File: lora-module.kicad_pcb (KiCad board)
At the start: 4 copper layers, 50 parts, among them J101 Conn_Coaxial, J102 Conn_ARM_SWD_TagConnect_TC203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, Q101 PMN48XP, U201 STM32WLE5CCUx, U301 BALFHB-WL-05D3, U302 BGS12SN6E6327XTSA1, U401 SST26VF080A

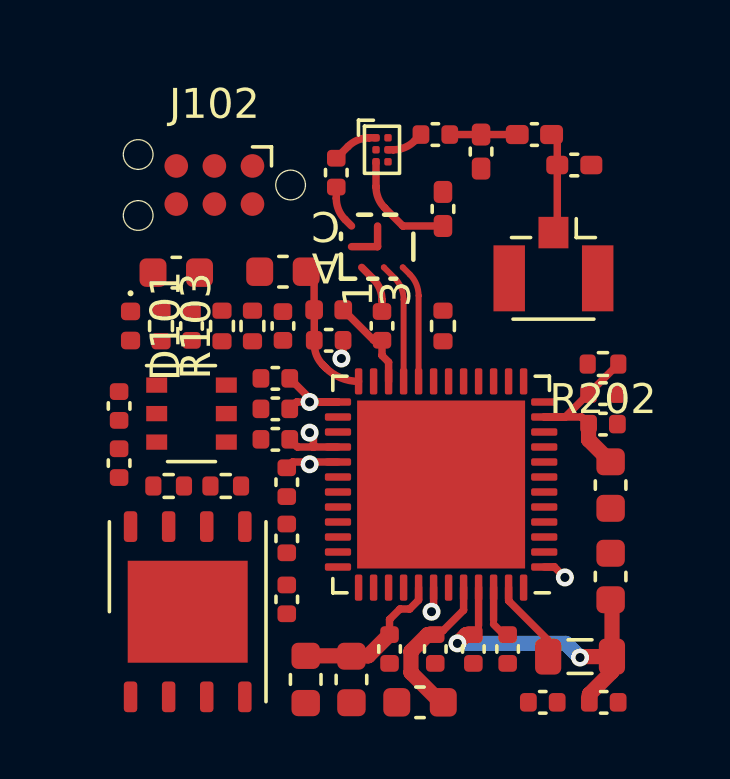
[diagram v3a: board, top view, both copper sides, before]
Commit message: added the crystal
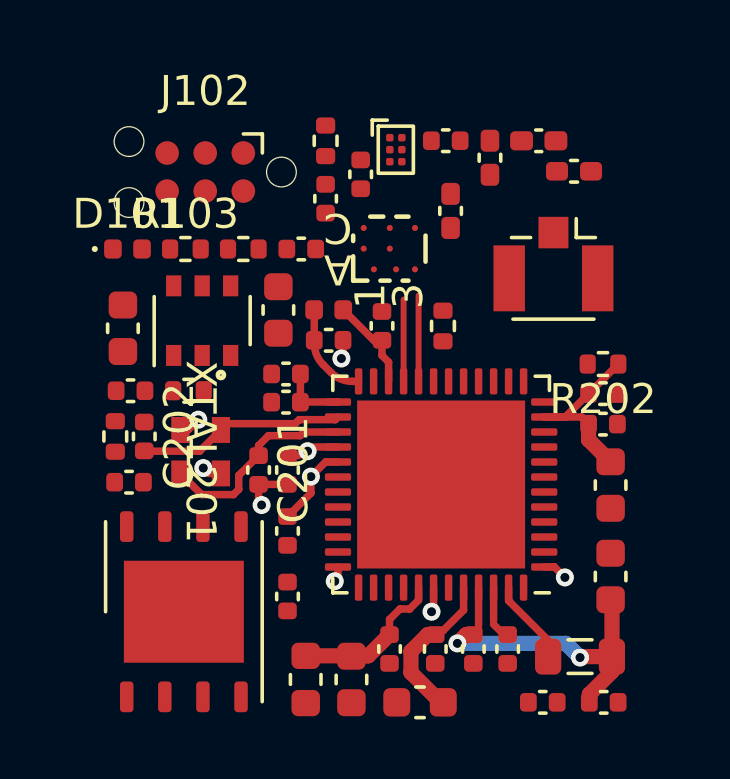
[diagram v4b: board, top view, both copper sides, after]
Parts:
- added C201: 6.8p, Capacitor_SMD:C_0402_1005Metric, F.Cu at (131.3, 101.4)
- added XTAL201: NX2016SA-32MHZ-EXS00A-CS11336, lora-module:NX2016SA_NDK, F.Cu at (129.3, 100.8)
- C202: value 100n -> 6.8
- moved C202 7.21 mm to (127.5, 100.3)
- moved R301 7.07 mm to (133.5, 90.5), turned to -90 degrees
- moved C307 6.16 mm to (133.5, 92.4)
- moved R102 3.41 mm to (128.9, 98.8)
- moved Q101 3.12 mm to (129.4, 96.5), turned to 90 degrees
- moved R103 2.69 mm to (128.8, 94.1), turned to 0 degrees
- moved C309 2.64 mm to (132.7, 94.1), turned to 0 degrees
- moved R302 2.58 mm to (130.8, 94.1), turned to 0 degrees
- moved C101 2.57 mm to (126.7, 96.7), turned to 90 degrees
- moved D101 2.57 mm to (126.9, 94.1), turned to 0 degrees
- moved R101 2.43 mm to (126.5, 100.3), turned to -90 degrees
- moved C204 1.94 mm to (132.2, 105.7)
- moved C213 1.63 mm to (132.2, 103.5)
- moved C301 1.28 mm to (131.9, 96.1), turned to 90 degrees
- moved C209 1.10 mm to (132.2, 101.4), turned to -90 degrees
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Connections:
- C202 pad 1: /STM32WL/VBAT -> GND
- C202 pad 2: GND -> Net-(U201-OSC_IN)
- U201 pad 26: unconnected-(U201-OSC_IN-Pad26) -> Net-(U201-OSC_IN)
- U201 pad 27: unconnected-(U201-OSC_OUT-Pad27) -> Net-(U201-OSC_OUT)
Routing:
- net Net-(U201-OSC_IN): track 0.00 -> 6.93 mm
- net Net-(U201-OSC_OUT): track 0.00 -> 6.88 mm
- net Net-(U301-RFI_IN): track 3.80 -> 0.00 mm
- net /RF frontend/RF_ANT: track 3.71 -> 0.00 mm
- net Net-(C310-Pad2): track 2.25 -> 0.00 mm
- net Net-(U301-RFO_IN): track 1.70 -> 0.00 mm
- net Net-(U302-RF2): track 1.56 -> 0.00 mm
- net GND: track 2.19 -> 3.73 mm, vias 1 -> 4
- net Net-(U301-RFO_OUT): track 1.46 -> 0.00 mm
- net /RF frontend/VR_PA: track 4.63 -> 3.27 mm
- net /RF frontend/RFI_N: track 4.02 -> 2.73 mm
- net Net-(U302-RF): track 1.26 -> 0.00 mm
- net /RF frontend/RFI_P: track 3.97 -> 2.86 mm
- net /STM32WL/VDDPA: track 16.8 -> 16.1 mm, vias 4 -> 3
- net /STM32WL/SWDIO: track 0.00 -> 0.52 mm, vias 0 -> 1

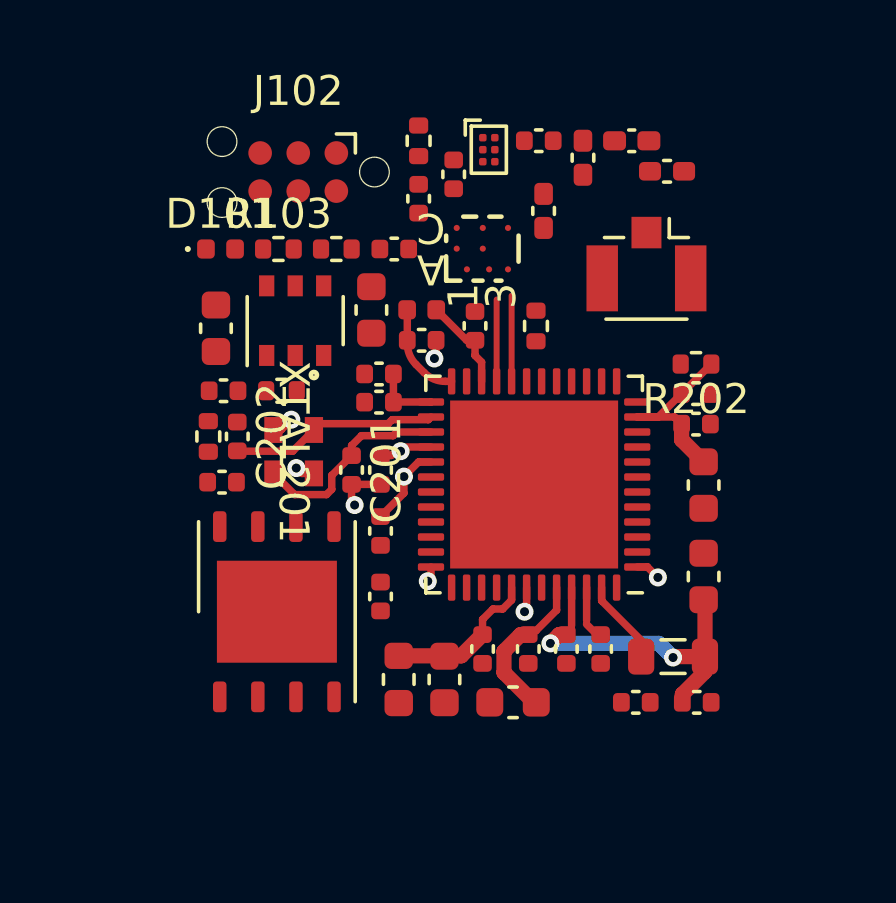
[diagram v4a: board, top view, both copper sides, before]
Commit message: added castellated edge connectors
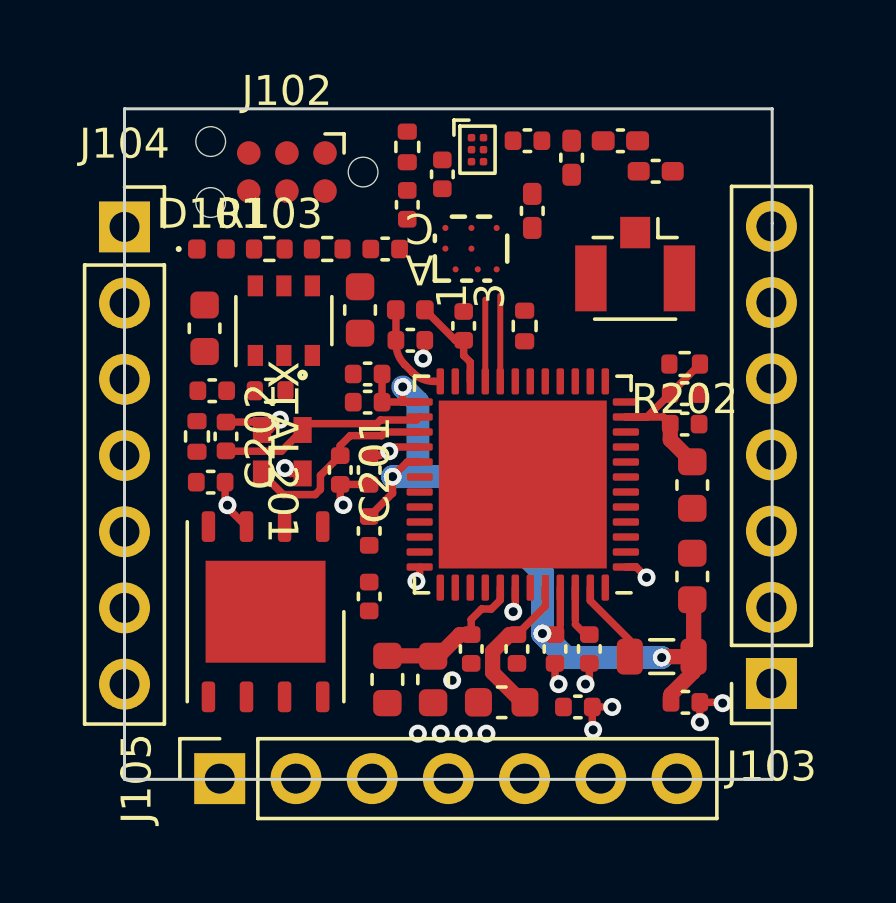
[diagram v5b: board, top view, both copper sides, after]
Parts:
- added J103: Conn_01x07_Socket, Connector_PinSocket_2.54mm:PinSocket_1x07_P2.54mm_Vertical, F.Cu at (145.3, 108.6)
- added J104: Conn_01x07_Socket, Connector_PinSocket_2.54mm:PinSocket_1x07_P2.54mm_Vertical, F.Cu at (123.7, 93.3)
- added J105: Conn_01x07_Socket, Connector_PinSocket_2.54mm:PinSocket_1x07_P2.54mm_Vertical, F.Cu at (126.9, 111.7)
- moved C218 1.94 mm to (138.8, 109.3)
- moved C307 0.43 mm to (133.1, 92.6)
- moved R301 0.43 mm to (133.1, 90.7)
- moved C201 0.38 mm to (130.9, 101.4)
- moved C203 0.38 mm to (136.3, 109.2)
- moved C204 0.38 mm to (131.9, 105.7)
- moved C209 0.38 mm to (131.9, 101.4)
- moved C210 0.38 mm to (135.3, 107.4)
- moved C211 0.38 mm to (142.6, 105.0)
- moved C213 0.38 mm to (131.9, 103.5)
- moved C214 0.38 mm to (142.6, 102.0)
- moved C215 0.38 mm to (131.8, 99.2)
- moved C217 0.38 mm to (131.8, 98.2)
- moved C220 0.38 mm to (136.8, 107.4)
- moved C301 0.38 mm to (131.5, 96.1)
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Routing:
- net /STM32WL/VDDPA: track 16.1 -> 28.8 mm, vias 3 -> 4
- net GND: track 3.73 -> 9.40 mm, vias 4 -> 15
- net VDD_SW: track 0.00 -> 1.85 mm, vias 0 -> 1
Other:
- board outline added: 21.6 x 22.4 mm

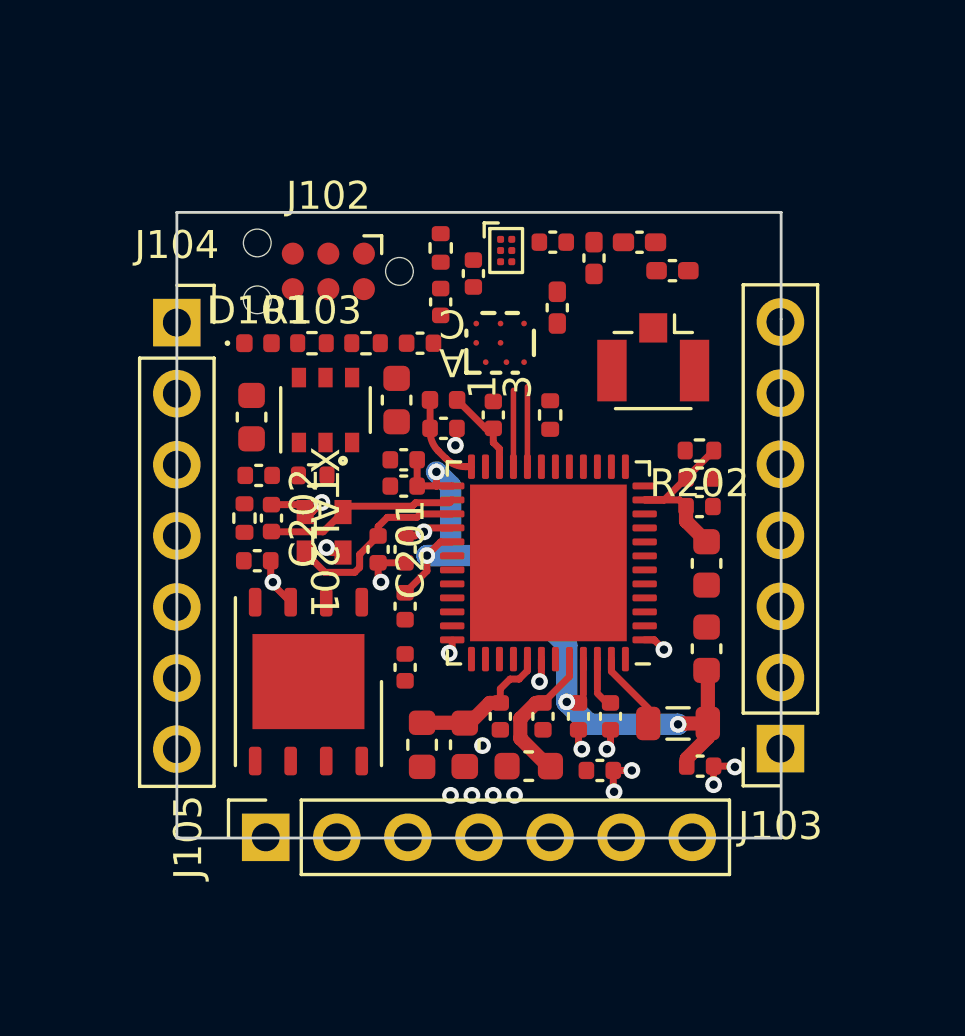
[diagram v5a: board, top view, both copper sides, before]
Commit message: created a footprint for the edge connectors
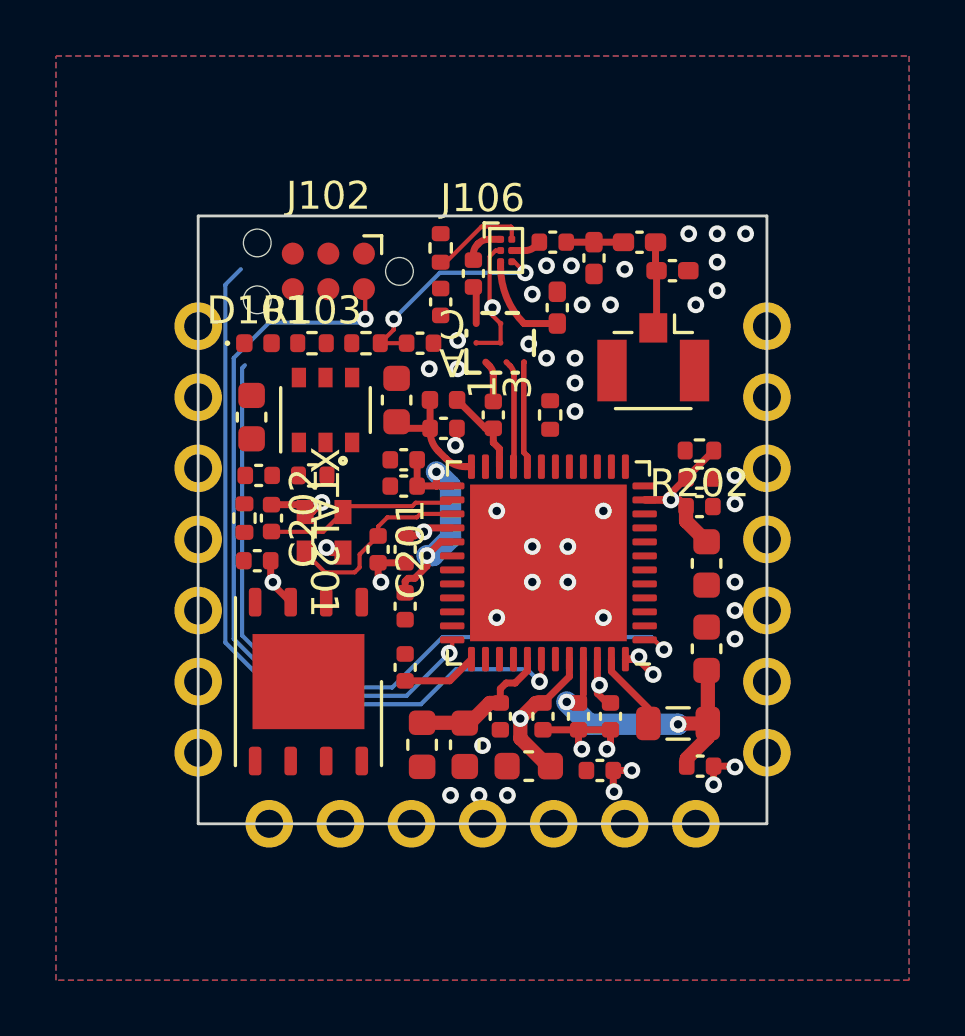
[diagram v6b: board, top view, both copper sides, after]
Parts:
- removed J103, J104, J105: Conn_01x07_Socket, Connector_PinSocket_2.54mm:PinSocket_1x07_P2.54mm_Vertical
- added J106: ~, lora-module:module-connectors, F.Cu at (134.6, 101.1)
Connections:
- net /STM32WL/BOOT0 renamed /BOOT0
- net /STM32WL/VBAT renamed /VBAT
- U201 pad 13: unconnected-(U201-PA5-Pad13) -> /FLASH/MISO
- U201 pad 16: unconnected-(U201-PA8-Pad16) -> /FLASH/SCK
- U201 pad 31: unconnected-(U201-PB2-Pad31) -> /FLASH/~{CS}
- U201 pad 32: unconnected-(U201-PB12-Pad32) -> /FLASH/~{HOLD}
- U201 pad 33: unconnected-(U201-PA10-Pad33) -> /FLASH/MOSI
- U401 pad 1: /EEPROM/~{CS} -> /FLASH/~{CS}
- U401 pad 2: /EEPROM/MISO -> /FLASH/MISO
- U401 pad 5: /EEPROM/MOSI -> /FLASH/MOSI
- U401 pad 6: /EEPROM/SCK -> /FLASH/SCK
- U401 pad 7: /EEPROM/~{HOLD} -> /FLASH/~{HOLD}
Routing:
- net /STM32WL/SWO: track 0.83 -> 27.3 mm
- net /STM32WL/SWCLK: track 0.83 -> 27.2 mm
- net /STM32WL/SWDIO: track 0.52 -> 26.1 mm, vias 1 -> 2
- net GND: track 9.40 -> 18.0 mm, vias 15 -> 48
- net Net-(U302-VDD): track 0.00 -> 8.03 mm, vias 0 -> 2
- net Net-(U301-RFI_IN): track 0.00 -> 3.60 mm
- net Net-(U302-CTRL): track 0.00 -> 3.51 mm
- net /RF frontend/RF_ANT: track 0.00 -> 3.12 mm
- net /VBAT: track 0.00 -> 2.69 mm
- net Net-(C310-Pad2): track 0.00 -> 2.05 mm
- net Net-(U301-RFO_IN): track 0.00 -> 1.49 mm
- net Net-(U302-RF2): track 0.00 -> 1.47 mm
- net Net-(U301-RFO_OUT): track 0.00 -> 1.35 mm
- net /RF frontend/VR_PA: track 3.27 -> 4.56 mm
- net /RF frontend/RFI_N: track 2.73 -> 3.83 mm
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- added copper zone on B.Cu, net GND
- added copper zone on F.Cu, net GND
- added copper zone on In1.Cu, net GND
- added copper zone on In2.Cu, net VDD
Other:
- board size 21.6 x 22.4 mm -> 20.3 x 21.7 mm

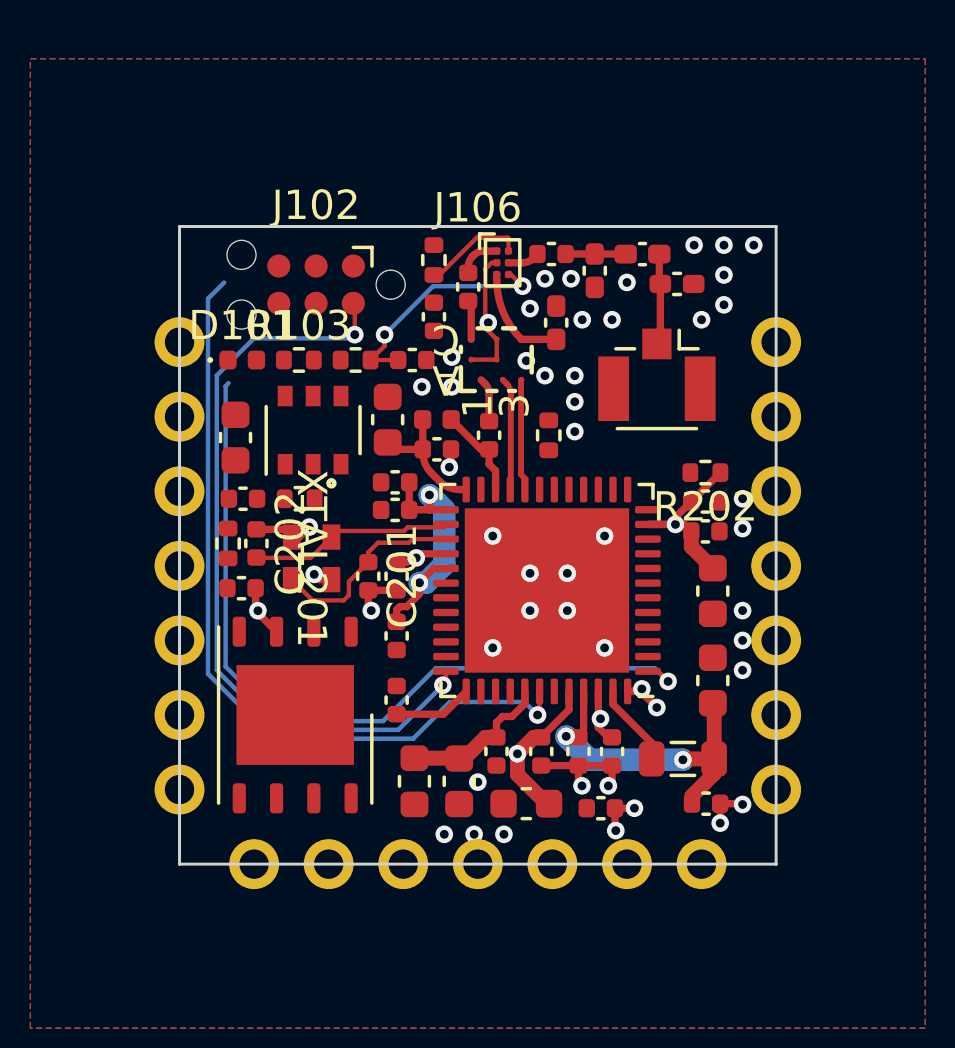
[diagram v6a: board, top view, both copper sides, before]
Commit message: mostly finishing, all IOs connected, drc clean
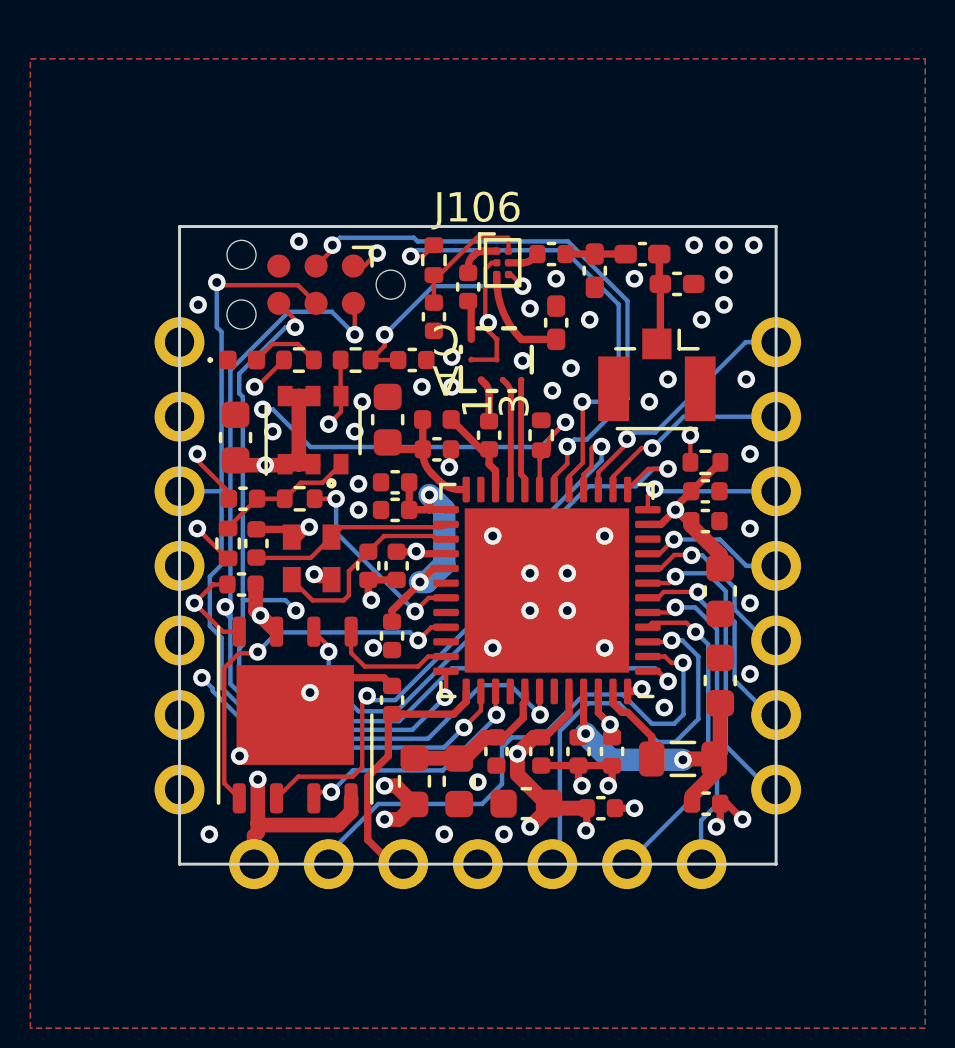
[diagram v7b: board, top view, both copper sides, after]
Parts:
- moved C201 0.36 mm to (130.9, 101.1)
- moved C209 0.36 mm to (131.9, 101.1)
- moved C207 0.35 mm to (142.4, 99.6)
- moved R202 0.35 mm to (142.4, 97.6)
- moved C216 0.35 mm to (142.4, 98.6)
- moved R201 0.26 mm to (136.8, 96.6)
- moved C211 0.25 mm to (142.9, 105.0)
- moved C214 0.25 mm to (142.9, 102.0)
- moved C204 0.16 mm to (131.7, 105.7)
- moved C213 0.16 mm to (131.7, 103.5)
- moved C401 0.13 mm to (126.6, 101.7)
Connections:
- J102 pad 2: /STM32WL/SWDIO -> /SWDIO
- J102 pad 3: /STM32WL/NRST -> /NRST
- J102 pad 4: /STM32WL/SWCLK -> /SWCLK
- J102 pad 6: /STM32WL/SWO -> /SWO
- J106 pad 1: unconnected-(J106-Pad1) -> /IO1
- J106 pad 10: unconnected-(J106-Pad10) -> /IO10
- J106 pad 11: unconnected-(J106-Pad11) -> GND
- J106 pad 12: unconnected-(J106-Pad12) -> /VBAT
- J106 pad 13: unconnected-(J106-Pad13) -> /IO11
- J106 pad 14: unconnected-(J106-Pad14) -> VDD_SW
- J106 pad 15: unconnected-(J106-Pad15) -> VDD
- J106 pad 16: unconnected-(J106-Pad16) -> GND
- J106 pad 17: unconnected-(J106-Pad17) -> /SWO
- J106 pad 18: unconnected-(J106-Pad18) -> /SWDIO
- J106 pad 19: unconnected-(J106-Pad19) -> /SWCLK
- J106 pad 2: unconnected-(J106-Pad2) -> /IO2
- J106 pad 20: unconnected-(J106-Pad20) -> /BOOT0
- J106 pad 21: unconnected-(J106-Pad21) -> /NRST
- J106 pad 3: unconnected-(J106-Pad3) -> /IO3
- J106 pad 4: unconnected-(J106-Pad4) -> /IO4
- J106 pad 5: unconnected-(J106-Pad5) -> /IO5
- J106 pad 6: unconnected-(J106-Pad6) -> /IO6
- J106 pad 7: unconnected-(J106-Pad7) -> /IO7
- J106 pad 8: unconnected-(J106-Pad8) -> /IO8
- J106 pad 9: unconnected-(J106-Pad9) -> /IO9
- R102 pad 2: unconnected-(R102-Pad2) -> /STM32WL/~{VDD_SW_EN}
- R103 pad 1: unconnected-(R103-Pad1) -> /STM32WL/LED
- R202 pad 2: /STM32WL/NRST -> /NRST
- U201 pad 1: /STM32WL/SWO -> /SWO
- U201 pad 12: unconnected-(U201-PA4-Pad12) -> /IO3
- U201 pad 14: unconnected-(U201-PA6-Pad14) -> /IO2
- U201 pad 15: unconnected-(U201-PA7-Pad15) -> /IO1
- U201 pad 17: unconnected-(U201-PA9-Pad17) -> /RF frontend/RF_CTRL
- U201 pad 18: /STM32WL/NRST -> /NRST
- U201 pad 2: unconnected-(U201-PB4-Pad2) -> /IO11
- U201 pad 3: unconnected-(U201-PB5-Pad3) -> /IO10
- U201 pad 31: /FLASH/~{CS} -> /STM32WL/~{VDD_SW_EN}
- U201 pad 32: /FLASH/~{HOLD} -> unconnected-(U201-PB12-Pad32)
- U201 pad 35: unconnected-(U201-PA12-Pad35) -> /FLASH/~{CS}
- U201 pad 36: /STM32WL/SWDIO -> /SWDIO
- U201 pad 38: unconnected-(U201-PC13-Pad38) -> /STM32WL/LED
- U201 pad 39: unconnected-(U201-PC14-Pad39) -> /FLASH/~{HOLD}
- U201 pad 4: unconnected-(U201-PB6-Pad4) -> /IO9
- U201 pad 42: /STM32WL/SWCLK -> /SWCLK
- U201 pad 5: unconnected-(U201-PB7-Pad5) -> /IO8
- U201 pad 6: unconnected-(U201-PB8-Pad6) -> /IO7
- U201 pad 7: unconnected-(U201-PA0-Pad7) -> /IO6
- U201 pad 8: unconnected-(U201-PA1-Pad8) -> /IO5
- U201 pad 9: unconnected-(U201-PA2-Pad9) -> /IO4
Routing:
- net /SWO: track 0.00 -> 37.4 mm, vias 0 -> 3
- net /SWCLK: track 0.00 -> 32.8 mm, vias 0 -> 2
- net /NRST: track 0.00 -> 32.4 mm, vias 0 -> 3
- net /SWDIO: track 0.00 -> 29.5 mm, vias 0 -> 3
- net /STM32WL/SWO: track 27.3 -> 0.00 mm, vias 1 -> 0
- net /STM32WL/SWCLK: track 27.2 -> 0.00 mm, vias 1 -> 0
- net /STM32WL/SWDIO: track 26.1 -> 0.00 mm, vias 2 -> 0
- net VDD_SW: track 1.85 -> 26.5 mm, vias 1 -> 3
- net /STM32WL/LED: track 0.00 -> 23.7 mm, vias 0 -> 3
- net /FLASH/SCK: track 0.00 -> 20.3 mm, vias 0 -> 2
- net /FLASH/MISO: track 0.00 -> 19.6 mm, vias 0 -> 2
- net /IO11: track 0.00 -> 19.0 mm, vias 0 -> 1
- net /BOOT0: track 0.00 -> 16.8 mm, vias 0 -> 2
- net /RF frontend/RF_CTRL: track 0.00 -> 16.5 mm, vias 0 -> 2
- net /IO10: track 0.00 -> 14.7 mm, vias 0 -> 1
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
